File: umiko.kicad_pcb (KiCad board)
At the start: 4 copper layers, 333.6 x 103.8 mm, 371 parts, among them J1 MJ-4PP-9, J2 MJ-4PP-9, J4 USB_C_Receptacle_USB2.0_16P_T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, J5 USB_C_Receptacle_USB2.0, Q1 2N7002VC-, Q2 2N7002VC-, SW1 SWITCH, U1 USBLC6-2P6, U2 TLV75533PDQNR, U3 W25Q128JVPIQ, U4 RP2040, U5 74LVC1T45, Y1 12MHz

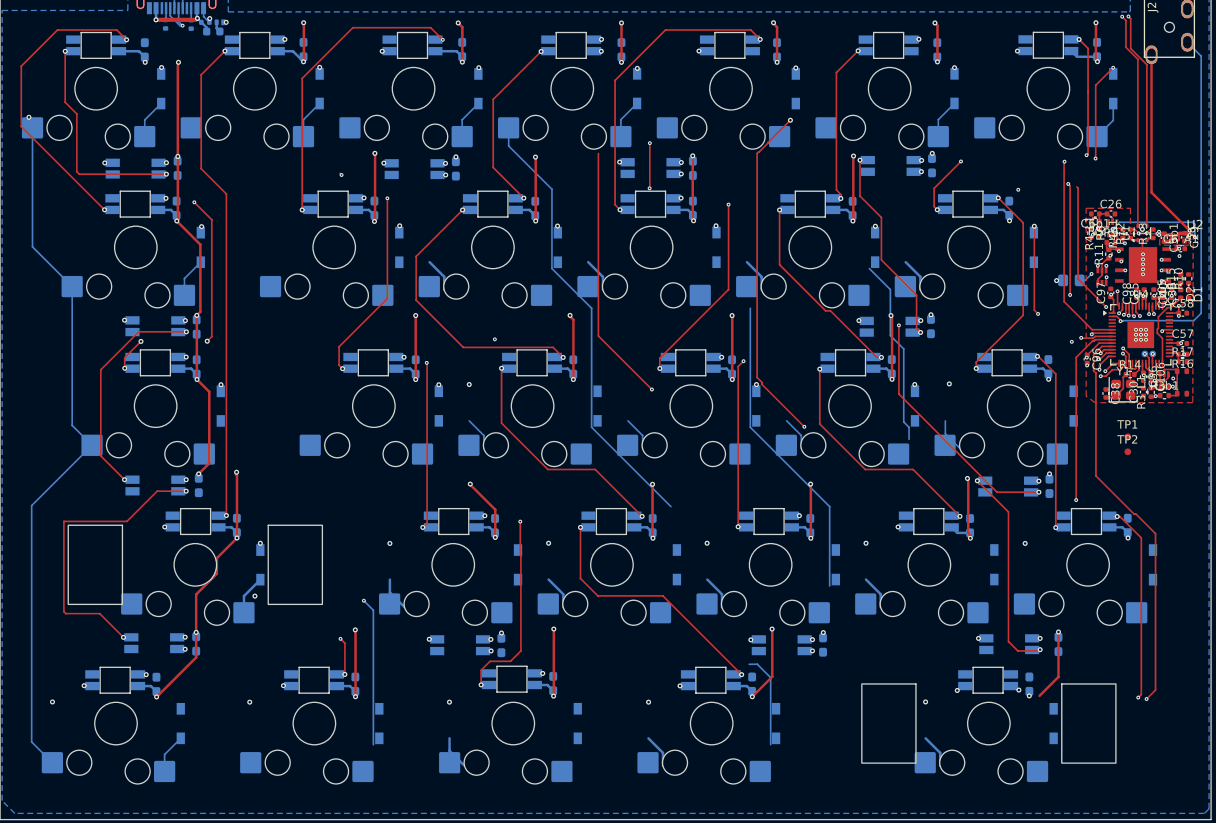
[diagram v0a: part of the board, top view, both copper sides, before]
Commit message: more tracing, left side only
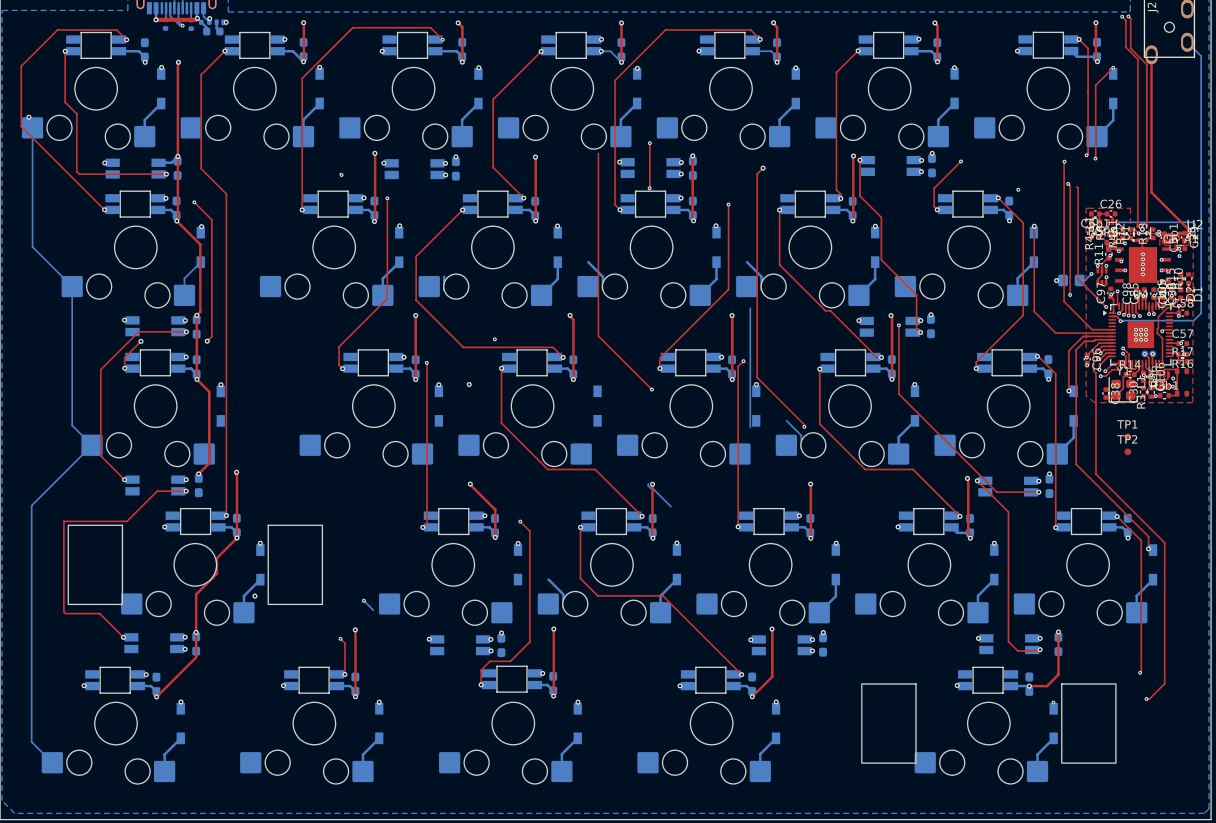
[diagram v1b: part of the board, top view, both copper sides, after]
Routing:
- net col3_L: track 163.7 -> 102.9 mm
- net col4_L: track 125.1 -> 88.3 mm
- net col2_L: track 86.1 -> 56.0 mm
- net row1_L: track 93.2 -> 122.8 mm, vias 8 -> 6
- net row2_L: track 88.3 -> 115.5 mm, vias 8 -> 6
- net col5_L: track 49.7 -> 27.2 mm
- net row3_L: track 125.8 -> 143.6 mm, vias 7 -> 6
- net Net-(D_12-A): track 35.8 -> 19.7 mm
- net +5V_L: track 960.4 -> 968.9 mm, vias 83 -> 81
- net row4_L: track 179.2 -> 171.0 mm
- net Net-(D_46-A): track 4.04 -> 8.84 mm
- net Net-(D_57-A): track 4.04 -> 8.84 mm
- net Net-(D_47-A): track 0.00 -> 4.79 mm
- net Net-(D_33-A): track 4.04 -> 8.83 mm
- net Net-(D_32-A): track 4.04 -> 8.83 mm
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
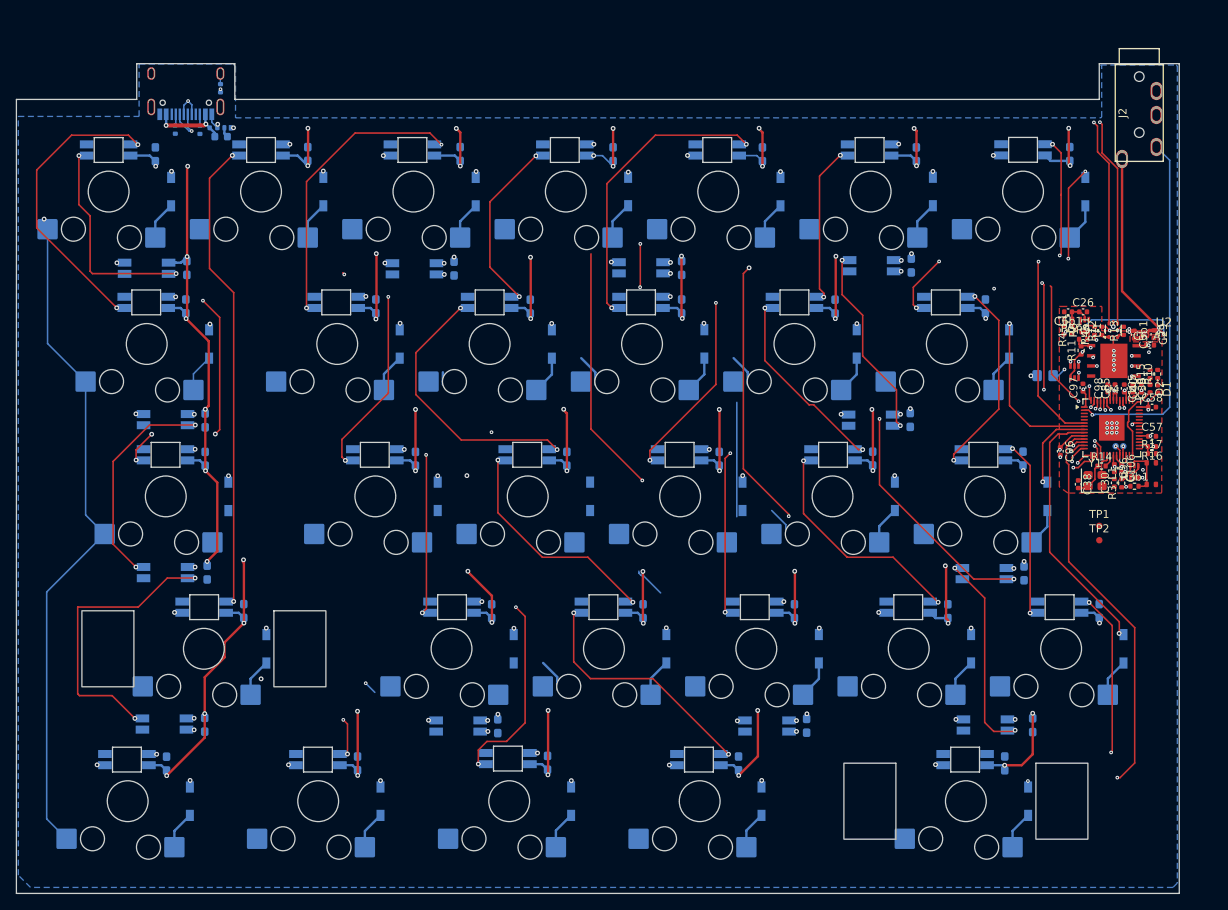
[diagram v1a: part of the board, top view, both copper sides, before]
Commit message: moving chips closer
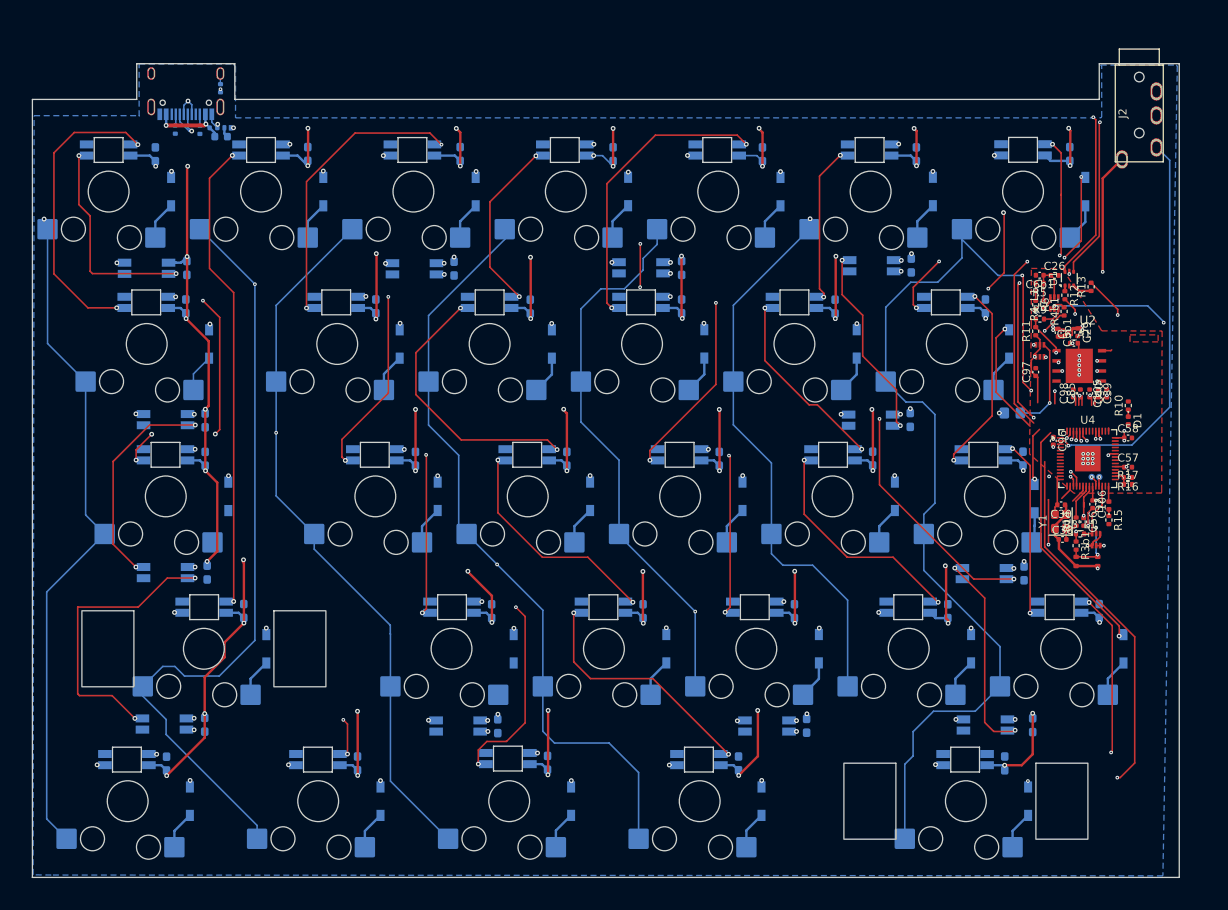
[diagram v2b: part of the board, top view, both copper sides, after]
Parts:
- removed the TP1 at (168.5, 87.5)
- removed the TP2 at (168.5, 89.3)
- moved R15 19.0 mm to (169.7, 86.8), turned to -90 degrees
- moved D2 15.5 mm to (169.7, 84.9), turned to 90 degrees
- moved SW1 13.6 mm to (167.0, 91.9), turned to 180 degrees
- moved R3b1 10.4 mm to (165.6, 90.0), turned to -90 degrees
- moved Q1 9.74 mm to (168.2, 89.2)
- moved C6_A1 9.52 mm to (165.4, 64.7)
- moved C29 9.52 mm to (165.9, 63.3)
- moved C5b1 9.52 mm to (163.4, 63.3)
- moved U2 9.52 mm to (164.6, 63.3)
- moved U1 8.48 mm to (164.8, 56.6)
- moved R3_L1 8.21 mm to (166.1, 88.5), turned to 0 degrees
- moved C56 7.73 mm to (166.6, 87.0)
- moved R14 7.64 mm to (165.7, 87.0), turned to 90 degrees
- moved C30 7.19 mm to (163.8, 84.9), turned to 180 degrees
- moved C38 7.18 mm to (164.0, 89.2), turned to 0 degrees
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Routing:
- net col2_L: track 56.0 -> 182.3 mm, vias 2 -> 1
- net col6_L: track 23.8 -> 127.7 mm, vias 2 -> 3
- net col1_L: track 112.5 -> 210.0 mm, vias 4 -> 3
- net col5_L: track 27.2 -> 122.9 mm, vias 2 -> 4
- net col3_L: track 102.9 -> 168.6 mm
- net col4_L: track 88.3 -> 125.9 mm, vias 3 -> 2
- net GND_L: track 8.79 -> 24.5 mm
- net Net-(D_12-A): track 19.7 -> 4.78 mm, vias 2 -> 0
- net Net-(Q1A-D): track 34.4 -> 48.6 mm
- net +3V3_L: track 34.7 -> 47.8 mm, vias 15 -> 14
- net /RGB_DO: track 17.8 -> 6.63 mm
- net +5V_L: track 968.9 -> 958.4 mm, vias 81 -> 82
- net /D+: track 12.4 -> 3.62 mm
- net /LED: track 9.52 -> 1.94 mm
- net LED_L: track 4.45 -> 11.8 mm, vias 2 -> 1
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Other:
- board size 333.6 x 103.8 mm -> 331.6 x 103.8 mm

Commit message: before claude
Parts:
- added C107: 10u, Capacitor_SMD:C_0402_1005Metric, F.Cu at (233.2, -24.6)
- added C108: 10u, Capacitor_SMD:C_0402_1005Metric, F.Cu at (233.2, -22.6)
- added C109: 15p, Capacitor_SMD:C_0402_1005Metric, F.Cu at (233.2, -20.6)
- added C110: 15p, Capacitor_SMD:C_0402_1005Metric, F.Cu at (233.2, -18.7)
- added C111: 1u, Capacitor_SMD:C_0402_1005Metric, F.Cu at (233.2, -16.7)
- added C112: 1u, Capacitor_SMD:C_0402_1005Metric, F.Cu at (233.2, -14.7)
- added C113: 100n, Capacitor_SMD:C_0402_1005Metric, F.Cu at (236.1, -26.6)
- added C114: 100n, Capacitor_SMD:C_0402_1005Metric, F.Cu at (236.1, -24.6)
- added C115: 100n, Capacitor_SMD:C_0402_1005Metric, F.Cu at (236.1, -22.6)
- added C116: 100n, Capacitor_SMD:C_0402_1005Metric, F.Cu at (236.1, -20.6)
- added C117: 100n, Capacitor_SMD:C_0402_1005Metric, F.Cu at (236.1, -18.7)
- added C118: 100n, Capacitor_SMD:C_0402_1005Metric, F.Cu at (236.1, -16.7)
- added C119: 100n, Capacitor_SMD:C_0402_1005Metric, F.Cu at (236.1, -14.7)
- added C120: 100n, Capacitor_SMD:C_0402_1005Metric, F.Cu at (239.0, -26.6)
- added C121: 100n, Capacitor_SMD:C_0402_1005Metric, F.Cu at (239.0, -24.6)
- added C5b2: 10u, Capacitor_SMD:C_0402_1005Metric, F.Cu at (239.0, -22.6)
- added C6: 10u, Capacitor_SMD:C_0402_1005Metric, F.Cu at (233.2, -26.6)
- added C6_A2: 100n, Capacitor_SMD:C_0402_1005Metric, F.Cu at (239.0, -20.6)
- added C6b2: 4.7u, Capacitor_SMD:C_0402_1005Metric, F.Cu at (239.0, -18.7)
- added D4: PMEG2010BELD, PCM_0xcb:SOD882D, F.Cu at (248.5, -3.00)
- added D5: Power LED, Diode_SMD:D_0402_1005Metric, F.Cu at (229.8, -5.97)
- added D6: User LED, Diode_SMD:D_0402_1005Metric, F.Cu at (229.8, -3.98)
- added F2: 500mA, Fuse:Fuse_0603_1608Metric, F.Cu at (225.1, -2.61)
- added FB2: 600R, Resistor_SMD:R_0402_1005Metric, F.Cu at (224.5, -26.5)
- added J3: USB_C_Receptacle_USB2.0, PCM_0xcb:USB_C_Receptacle_HRO_TYPE-C-31-M-12, F.Cu at (237.6, -7.96)
- added Q3: 2N7002VC-, PCM_0xcb:SOT-563, F.Cu at (245.3, -12.1)
- added Q4: 2N7002VC-, PCM_0xcb:SOT-563, F.Cu at (245.3, -8.88)
- added R18: 5.1k, Resistor_SMD:R_0402_1005Metric, F.Cu at (224.5, -20.6)
- added R19: 5.1k, Resistor_SMD:R_0402_1005Metric, F.Cu at (224.5, -18.6)
- added R20: 1k, Resistor_SMD:R_0402_1005Metric, F.Cu at (224.5, -16.6)
- added R21: 1k, Resistor_SMD:R_0402_1005Metric, F.Cu at (224.5, -14.6)
- added R22: 10k, Resistor_SMD:R_0402_1005Metric, F.Cu at (227.4, -26.5)
- added R23: 27, Resistor_SMD:R_0402_1005Metric, F.Cu at (227.4, -24.6)
- added R24: 27, Resistor_SMD:R_0402_1005Metric, F.Cu at (227.4, -22.6)
- added R25: 1k, Resistor_SMD:R_0402_1005Metric, F.Cu at (227.4, -20.6)
- added R26: 1k, Resistor_SMD:R_0402_1005Metric, F.Cu at (227.4, -18.6)
- added R27: 5.1k, Resistor_SMD:R_0402_1005Metric, F.Cu at (227.4, -16.6)
- added R28: 10k, Resistor_SMD:R_0402_1005Metric, F.Cu at (227.4, -14.6)
- added R3: 51k, Resistor_SMD:R_0402_1005Metric, F.Cu at (224.5, -24.6)
- added R3_L2: 10k, Resistor_SMD:R_0402_1005Metric, F.Cu at (230.3, -26.5)
- added R3b2: 10k, Resistor_SMD:R_0402_1005Metric, F.Cu at (230.3, -24.6)
- added R4: 51k, Resistor_SMD:R_0402_1005Metric, F.Cu at (224.5, -22.6)
- added R4_L2: 51k, Resistor_SMD:R_0402_1005Metric, F.Cu at (230.3, -22.6)
- added R4b2: 10k, Resistor_SMD:R_0402_1005Metric, F.Cu at (230.3, -20.6)
- added SW2: SWITCH, PCM_0xcb:1.9x2.8mm SW, F.Cu at (225.6, -5.41)
- added TP1: CLK, PCM_0xcb:TestPoint_Pad_D0.8mm, F.Cu at (248.1, -12.9)
- added TP2: DIO, PCM_0xcb:TestPoint_Pad_D0.8mm, F.Cu at (248.1, -11.1)
- added TP3: CLK, PCM_0xcb:TestPoint_Pad_D0.8mm, F.Cu at (248.1, -9.25)
- added TP4: DIO, PCM_0xcb:TestPoint_Pad_D0.8mm, F.Cu at (248.1, -7.45)
- added U10: 74LVC1T45, PCM_0xcb:SOT-563, F.Cu at (245.3, -5.63)
- added U6: USBLC6-2P6, Package_TO_SOT_SMD:SOT-666, F.Cu at (247.0, -16.4)
- added U7: TLV75533PDQNR, PCM_0xcb:X2SON-4, F.Cu at (248.7, -5.28)
- added U8: W25Q128JVPIQ, PCM_0xcb:W25Q128JVPIQ, F.Cu at (227.6, -10.3)
- added U9: RP2040, Package_DFN_QFN:QFN-56-1EP_7x7mm_P0.4mm_EP3.2x3.2mm, F.Cu at (245.4, -22.9)
- added Y2: 12MHz, Crystal:Crystal_SMD_2520-4Pin_2.5x2.0mm, F.Cu at (242.7, -16.2)
- SW_1, SW_18, SW_19, SW_2, SW_20, SW_21, SW_22, SW_23, SW_24, SW_25, SW_3, SW_35, SW_36, SW_37, SW_38, SW_39, SW_4, SW_40, SW_41, SW_48, SW_49, SW_5, SW_50, SW_51, SW_52, SW_53, SW_6, SW_61, SW_62, SW_63, SW_64, SW_65, SW_7: moved to B.Cu
- moved C4 160.5 mm to (336.1, -5.53)
- moved LED3 160.5 mm to (299.2, -0.02)
- moved LED4 160.5 mm to (329.3, -14.9)
- moved R1 160.5 mm to (285.6, -1.76)
- moved RSW1 160.5 mm to (298.1, 16.4)
- moved C39 3.57 mm to (169.7, 74.3)
- moved C40 3.57 mm to (168.6, 74.3)
- moved C98 3.57 mm to (166.6, 74.3)
- moved C85 3.57 mm to (167.5, 74.3)
- moved C105 3.50 mm to (170.5, 74.3)
- moved R13 2.40 mm to (165.4, 58.7), turned to -90 degrees
- moved D1 1.07 mm to (171.7, 75.3)
- moved R10 1.07 mm to (171.7, 73.4)
- moved C96 1.00 mm to (162.7, 75.9), turned to 90 degrees
- moved D_47 1.00 mm to (160.5, 85.1)
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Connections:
- C1 pad 1: 5V_R -> +5V_R
- C104 pad 1: 5V_R -> +5V_R
- C14 pad 1: 5V_R -> +5V_R
- C2 pad 1: 5V_R -> +5V_R
- C20 pad 2: 5V_R -> +5V_R
- C21 pad 1: 5V_R -> +5V_R
- C22 pad 2: 5V_R -> +5V_R
- C23 pad 2: 5V_R -> +5V_R
- C24 pad 1: 5V_R -> +5V_R
- C25 pad 2: 5V_R -> +5V_R
- C27 pad 1: 5V_R -> +5V_R
- C28 pad 2: 5V_R -> +5V_R
- C3 pad 1: 5V_R -> +5V_R
- C31 pad 1: 5V_R -> +5V_R
- C32 pad 1: 5V_R -> +5V_R
- C33 pad 1: 5V_R -> +5V_R
- C34 pad 1: 5V_R -> +5V_R
- C35 pad 1: 5V_R -> +5V_R
- C36 pad 1: 5V_R -> +5V_R
- C37 pad 1: 5V_R -> +5V_R
- C4 pad 1: 5V_R -> +5V_R
- C48 pad 1: 5V_R -> +5V_R
- C49 pad 1: 5V_R -> +5V_R
- C50 pad 1: 5V_R -> +5V_R
- C51 pad 1: 5V_R -> +5V_R
- C52 pad 1: 5V_R -> +5V_R
- C53 pad 1: 5V_R -> +5V_R
- C54 pad 1: 5V_R -> +5V_R
- C55 pad 1: 5V_R -> +5V_R
- C65 pad 1: 5V_R -> +5V_R
- C66 pad 1: 5V_R -> +5V_R
- C67 pad 1: 5V_R -> +5V_R
- C68 pad 1: 5V_R -> +5V_R
- C69 pad 1: 5V_R -> +5V_R
- C70 pad 1: 5V_R -> +5V_R
- C71 pad 1: 5V_R -> +5V_R
- C79 pad 1: 5V_R -> +5V_R
- C80 pad 1: 5V_R -> +5V_R
- C81 pad 1: 5V_R -> +5V_R
- C82 pad 1: 5V_R -> +5V_R
- C83 pad 1: 5V_R -> +5V_R
- C84 pad 1: 5V_R -> +5V_R
- C91 pad 1: 5V_R -> +5V_R
- C92 pad 1: 5V_R -> +5V_R
- C93 pad 1: 5V_R -> +5V_R
- C94 pad 1: 5V_R -> +5V_R
- C95 pad 1: 5V_R -> +5V_R
- D_1 pad 1: row0_R -> row0_L
- D_18 pad 1: row1_R -> row1_L
- D_19 pad 1: row1_R -> row1_L
- D_2 pad 1: row0_R -> row0_L
- D_20 pad 1: row1_R -> row1_L
- D_21 pad 1: row1_R -> row1_L
- D_22 pad 1: row1_R -> row1_L
- D_23 pad 1: row1_R -> row1_L
- D_24 pad 1: row1_R -> row1_L
- D_25 pad 1: row1_R -> row1_L
- D_3 pad 1: row0_R -> row0_L
- D_35 pad 1: row2_R -> row2_L
- D_36 pad 1: row2_R -> row2_L
- D_37 pad 1: row2_R -> row2_L
- D_38 pad 1: row2_R -> row2_L
- D_39 pad 1: row2_R -> row2_L
- D_4 pad 1: row0_R -> row0_L
- D_40 pad 1: row2_R -> row2_L
- D_41 pad 1: row2_R -> row2_L
- D_48 pad 1: row3_R -> row3_L
- D_49 pad 1: row3_R -> row3_L
- D_5 pad 1: row0_R -> row0_L
- D_50 pad 1: row3_R -> row3_L
- D_51 pad 1: row3_R -> row3_L
- D_52 pad 1: row3_R -> row3_L
- D_53 pad 1: row3_R -> row3_L
- D_6 pad 1: row0_R -> row0_L
- D_61 pad 1: row4_R -> row4_L
- D_62 pad 1: row4_R -> row4_L
- D_63 pad 1: row4_R -> row4_L
- D_64 pad 1: row4_R -> row4_L
- D_65 pad 1: row4_R -> row4_L
- D_7 pad 1: row0_R -> row0_L
- J1 pad 1: unconnected-(J1-A-Pad1) -> +5V_R
- J1 pad 2: unconnected-(J1-B-Pad2) -> GND_R
- J1 pad 4: data_R -> data_L
- LED1 pad 1: 5V_R -> +5V_R
- LED104 pad 1: 5V_R -> +5V_R
- LED14 pad 1: 5V_R -> +5V_R
- LED15 pad 1: 5V_R -> +5V_R
- LED16 pad 1: 5V_R -> +5V_R
- LED17 pad 1: 5V_R -> +5V_R
- LED18 pad 1: 5V_R -> +5V_R
- LED19 pad 1: 5V_R -> +5V_R
- LED2 pad 1: 5V_R -> +5V_R
- LED20 pad 1: 5V_R -> +5V_R
- LED22 pad 1: 5V_R -> +5V_R
- LED23 pad 1: 5V_R -> +5V_R
- LED3 pad 1: 5V_R -> +5V_R
- LED31 pad 1: 5V_R -> +5V_R
- LED32 pad 1: 5V_R -> +5V_R
- LED33 pad 1: 5V_R -> +5V_R
- LED34 pad 1: 5V_R -> +5V_R
- LED35 pad 1: 5V_R -> +5V_R
- LED36 pad 1: 5V_R -> +5V_R
- LED37 pad 1: 5V_R -> +5V_R
- LED4 pad 1: 5V_R -> +5V_R
- LED48 pad 1: 5V_R -> +5V_R
- LED49 pad 1: 5V_R -> +5V_R
- LED50 pad 1: 5V_R -> +5V_R
- LED51 pad 1: 5V_R -> +5V_R
- LED52 pad 1: 5V_R -> +5V_R
- LED53 pad 1: 5V_R -> +5V_R
- LED54 pad 1: 5V_R -> +5V_R
- LED55 pad 1: 5V_R -> +5V_R
- LED65 pad 1: 5V_R -> +5V_R
- LED66 pad 1: 5V_R -> +5V_R
- LED67 pad 1: 5V_R -> +5V_R
- LED68 pad 1: 5V_R -> +5V_R
- LED69 pad 1: 5V_R -> +5V_R
- LED70 pad 1: 5V_R -> +5V_R
- LED71 pad 1: 5V_R -> +5V_R
- LED79 pad 1: 5V_R -> +5V_R
- LED80 pad 1: 5V_R -> +5V_R
- LED81 pad 1: 5V_R -> +5V_R
- LED82 pad 1: 5V_R -> +5V_R
- LED83 pad 1: 5V_R -> +5V_R
- LED84 pad 1: 5V_R -> +5V_R
- LED91 pad 1: 5V_R -> +5V_R
- LED92 pad 1: 5V_R -> +5V_R
- LED93 pad 1: 5V_R -> +5V_R
- LED94 pad 1: 5V_R -> +5V_R
- LED95 pad 1: 5V_R -> +5V_R
- SW_1 pad 1: col0_R -> col0_L
- SW_18 pad 1: col0_R -> col0_L
- SW_19 pad 1: col1_R -> col1_L
- SW_2 pad 1: col1_R -> col1_L
- SW_20 pad 1: col2_R -> col2_L
- SW_21 pad 1: col3_R -> col3_L
- SW_22 pad 1: col4_R -> col4_L
- SW_23 pad 1: col5_R -> col5_L
- SW_24 pad 1: col6_R -> col6_L
- SW_3 pad 1: col2_R -> col2_L
- SW_35 pad 1: col0_R -> col0_L
- SW_36 pad 1: col1_R -> col1_L
- SW_37 pad 1: col2_R -> col2_L
- SW_38 pad 1: col3_R -> col3_L
- SW_39 pad 1: col4_R -> col4_L
- SW_4 pad 1: col3_R -> col3_L
- SW_40 pad 1: col5_R -> col5_L
- SW_41 pad 1: col6_R -> col6_L
- SW_48 pad 1: col0_R -> col0_L
- SW_49 pad 1: col1_R -> col1_L
- SW_5 pad 1: col4_R -> col4_L
- SW_50 pad 1: col2_R -> col2_L
- SW_51 pad 1: col3_R -> col3_L
- SW_52 pad 1: col4_R -> col4_L
- SW_53 pad 1: col6_R -> col6_L
- SW_6 pad 1: col5_R -> col5_L
- SW_61 pad 1: col0_R -> col0_L
- SW_62 pad 1: col3_R -> col3_L
- SW_63 pad 1: col4_R -> col4_L
- SW_64 pad 1: col6_R -> col6_L
- U4 pad 19: GND -> GND_L
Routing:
- net /D+: track 3.62 -> 21.8 mm
- net col1_L: track 210.0 -> 222.6 mm, vias 3 -> 4
- net /D-: track 10.2 -> 21.7 mm
- net col5_L: track 122.9 -> 134.1 mm
- net col6_L: track 127.7 -> 138.5 mm
- net /RGB_DO: track 6.63 -> 16.8 mm
- net col2_L: track 182.3 -> 192.4 mm, vias 1 -> 2
- net row0_L: track 154.9 -> 163.3 mm
- net col0_L: track 232.6 -> 240.2 mm, vias 3 -> 4
- net row1_L: track 116.4 -> 123.8 mm
- net +5V_L: track 958.4 -> 965.6 mm
- net +3V3_L: track 47.8 -> 41.8 mm, vias 14 -> 15
- net Net-(Q1A-D): track 48.6 -> 44.5 mm
- net /QSPI_CS: track 11.7 -> 15.8 mm
- net /QSPI_SD3: track 12.5 -> 16.2 mm
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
